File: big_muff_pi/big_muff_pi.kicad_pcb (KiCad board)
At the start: 2 copper layers, 80 x 100 mm, 82 parts, among them J1 Jack_6.35, J2 Jack_6.35, J6 top_panel_connector, J7 Conn_01x01_Socket, J8 Conn_01x01_Socket, J9 Barrel_Jack_Switch, P1 big_muff_pi_front_panel, P2 bottom_panel, Q1 MMBT5551, Q10 AO3401A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

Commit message: small.
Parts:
- P1: value big_muff_pi_front_panel -> front_panel; footprint pedale:big_muff_pi_front_plate -> pedale:front_plate
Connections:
- J1 pad R: 0 -> unconnected-(J1-PadR)
- J2 pad R: 0 -> unconnected-(J2-PadR)
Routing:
- net BAT+: track 15.5 -> 5.66 mm
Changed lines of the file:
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@@
 	(net 48 "REG_IN")
 	(net 49 "Net-(Q12-D)")
+	(net 50 "unconnected-(J1-PadR)")
+	(net 51 "unconnected-(J2-PadR)")
 	(footprint "Resistor_SMD:R_0603_1608Metric_Pad0.98x0.95mm_HandSolder"
 		(layer "F.Cu")
@@
 			(net 43 "unconnected-(J6G-Pin_11-Pad11)")
 			(pinfunction "Pin_11")
-			(pintype "passive")
+			(pintype "passive+no_connect")
 		)
 		(pad "12" thru_hole circle
@@
 			(net 44 "unconnected-(J6G-Pin_13-Pad13)")
 			(pinfunction "Pin_13")
-			(pintype "passive")
+			(pintype "passive+no_connect")
 		)
 		(pad "14" thru_hole circle
@@
 			(net 45 "unconnected-(J6G-Pin_15-Pad15)")
 			(pinfunction "Pin_15")
-			(pintype "passive")
+			(pintype "passive+no_connect")
 		)
 		(pad "16" thru_hole circle
@@
 			(remove_unused_layers no)
 			(roundrect_rratio 0.3)
-			(net 13 "0")
+			(net 51 "unconnected-(J2-PadR)")
 			(pintype "passive")
 			(thermal_bridge_angle 45)
@@
 			(remove_unused_layers no)
 			(roundrect_rratio 0.3)
-			(net 13 "0")
+			(net 50 "unconnected-(J1-PadR)")
 			(pintype "passive")
 			(thermal_bridge_angle 45)
@@
 		(embedded_fonts no)
 	)
-	(footprint "pedale:big_muff_pi_front_plate"
+	(footprint "pedale:front_plate"
 		(layer "F.Cu")
 		(at 50 50)
@@
 			)
 		)
-		(property "Value" "big_muff_pi_front_panel"
+		(property "Value" "front_panel"
 			(at 0 1 0)
 			(unlocked yes)
@@
 	)
 	(segment
-		(start 68.9 89.48185)
-		(end 69.16815 89.75)
-		(width 0.5)
-		(layer "F.Cu")
-		(net 24)
-	)
-	(segment
 		(start -8 107.5)
 		(end -7 108.5)
@@
 	)
 	(segment
-		(start 74.9 89.75)
-		(end 75 89.65)
-		(width 0.5)
-		(layer "F.Cu")
-		(net 24)
-	)
-	(segment
-		(start 68.9 85.9)
-		(end 68.9 89.48185)
-		(width 0.5)
-		(layer "F.Cu")
-		(net 24)
-	)
-	(segment
 		(start -8.65 107.5)
 		(end -8 107.5)
@@
 		(width 0.5)
 		(layer "F.Cu")
-		(net 24)
-	)
-	(segment
-		(start 69.16815 89.75)
-		(end 74.9 89.75)
-		(width 0.5)
-		(layer "F.Cu")

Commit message: I LOVE U
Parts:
- moved C14 74.1 mm to (61.8, 99.5)
- moved C16 74.1 mm to (62.7, 93.6)
- moved C17 74.1 mm to (62.7, 91.9)
- moved C18 74.1 mm to (61.8, 101.0)
- moved C19 74.1 mm to (56.5, 92.5)
- moved C20 74.1 mm to (58.5, 104.6)
- moved Q5 74.1 mm to (60.0, 96.9)
- moved R24 74.1 mm to (56.6, 100.2)
- moved R27 44.6 mm to (62.5, 83.8)
- moved Q6 42.9 mm to (59.5, 76.0), turned to 90 degrees
- moved R23 41.1 mm to (59.5, 79.5), turned to 180 degrees
- moved Q12 39.7 mm to (58.8, 82.8), turned to 90 degrees
- moved R25 27.3 mm to (107.5, 52.0), turned to 180 degrees
- moved R26 20.0 mm to (101.8, 72.2)
- moved C2 2.12 mm to (76.4, 68.1)
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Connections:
- Q6 pad 2: REG_IN -> BAT+
- Q6 pad 3: BAT+ -> REG_IN
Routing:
- net IN_CONNECT: track 0.00 -> 121.5 mm, vias 0 -> 2
- net 9V: track 111.7 -> 214.8 mm, vias 5 -> 6
- net SW_IN: track 22.0 -> 103.7 mm, vias 4 -> 7
- net Net-(SW1B-B): track 0.00 -> 62.0 mm, vias 2 -> 0
- net BAT-: track 0.00 -> 60.1 mm, vias 0 -> 1
- net Net-(J6C-Pin_14): track 20.7 -> 76.6 mm, vias 4 -> 3
- net Net-(J6D-Pin_8): track 0.00 -> 37.1 mm, vias 0 -> 1
- net Net-(J6A-Pin_4): track 5.21 -> 38.8 mm
- net Net-(SW1A-B): track 0.00 -> 28.3 mm
- net BAT+: track 5.66 -> 31.1 mm
- net Net-(J6C-Pin_12): track 2.64 -> 26.4 mm
- net F_OUT: track 0.00 -> 21.8 mm
- net REG_IN: track 26.9 -> 47.2 mm
- net Net-(J6E-Pin_10): track 0.00 -> 17.2 mm
- net FS_OUT: track 0.00 -> 12.7 mm
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
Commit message: small mods.
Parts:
- removed SIM1: Logo_Open_Hardware_Small, Symbol:OSHW-Logo2_7.3x6mm_SilkScreen
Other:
- board text removed: "BMF"
- board text removed: "ostojaatanasijevic"

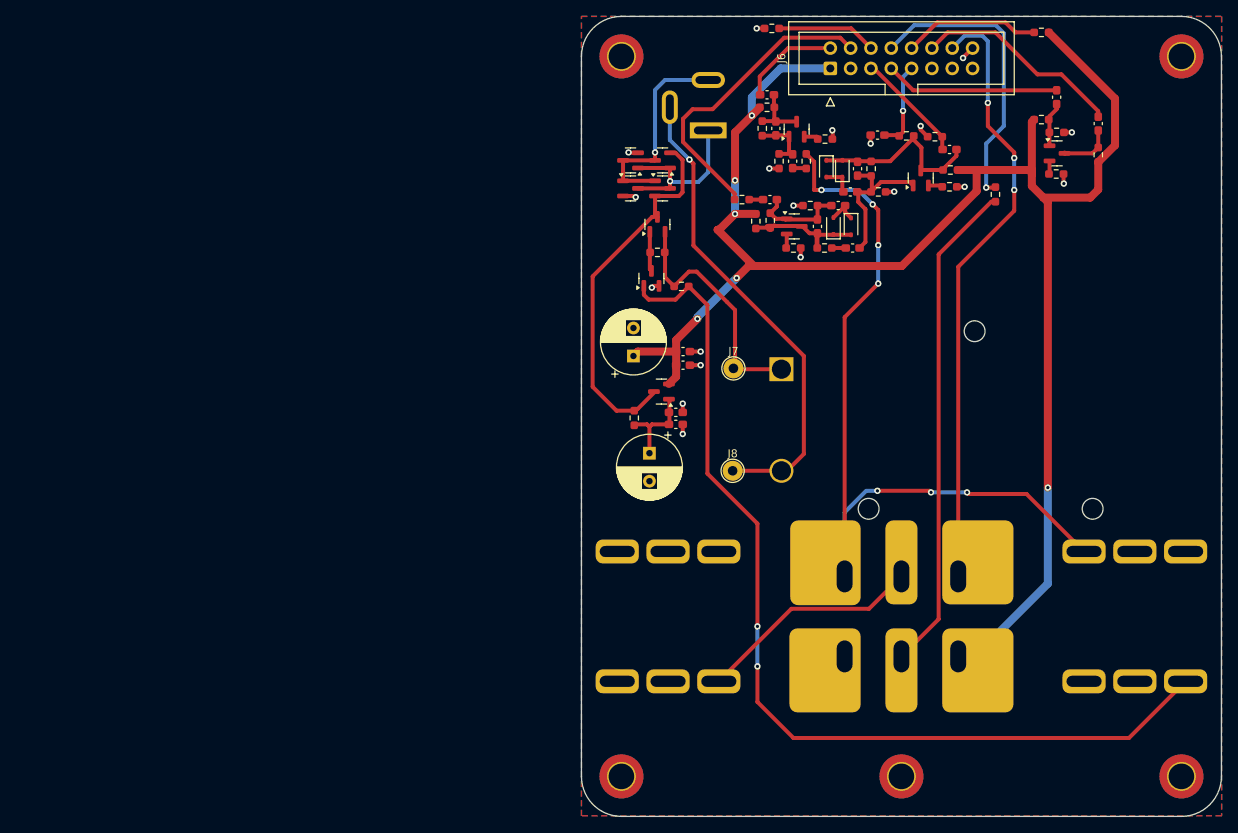
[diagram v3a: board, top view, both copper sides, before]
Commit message: New switch, fixed courtyards.
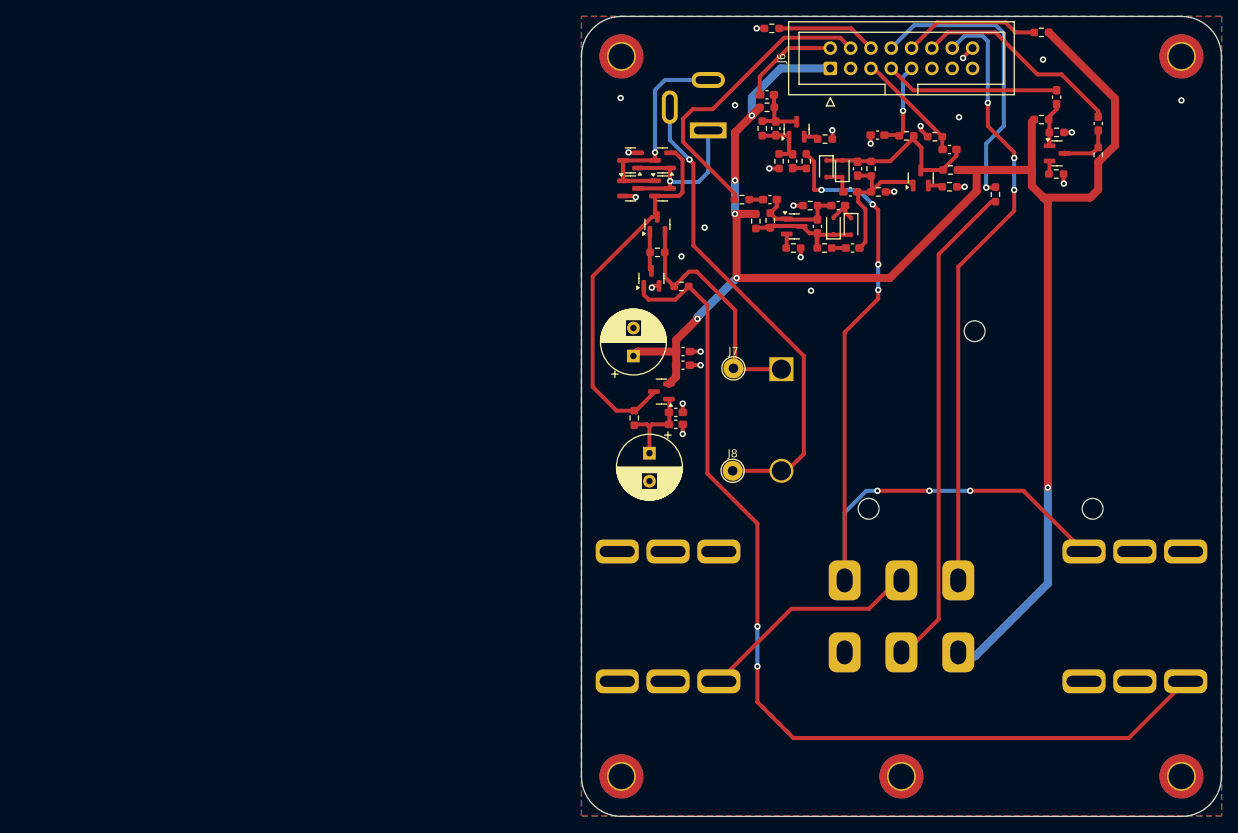
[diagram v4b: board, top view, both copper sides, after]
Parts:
- removed RV4, RV5, RV6: floating_pot, pedale:floating_pot
- SW1: footprint pedale:foot_switch_tht_and_floating -> pedale:foot_switch_tht_no_pad
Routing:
- net 9V: track 214.8 -> 213.5 mm
- net 0: vias 19 -> 27

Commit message: Updated traces.
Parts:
- moved Q10 3.57 mm to (56.7, 68.8)
- moved Q13 3.57 mm to (52.7, 72.3)
- moved Q14 3.57 mm to (52.7, 68.8)
- moved Q8 3.57 mm to (56.7, 72.3)
- moved R27 1.33 mm to (61.4, 84.5), turned to -90 degrees
- moved R23 0.45 mm to (59.7, 79.9)
- moved Q6 0.32 mm to (59.6, 76.3)
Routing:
- net IN_CONNECT: track 121.5 -> 111.1 mm
- net SW_IN: track 103.7 -> 96.8 mm
- net Net-(J6A-Pin_4): track 38.5 -> 31.7 mm
- net CONN-: track 26.5 -> 29.1 mm, vias 1 -> 0
- net BAT+: track 31.1 -> 29.3 mm
- net 9V: track 213.5 -> 212.5 mm
- net BAT-: track 60.1 -> 60.9 mm, vias 1 -> 0
- net CONN+: track 21.1 -> 21.9 mm
- net Net-(SW1A-B): track 28.3 -> 28.8 mm

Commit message: Main board almost ready.
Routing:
- net 0: track 22.2 -> 20.5 mm, vias 27 -> 29
- net Net-(Q2-B): track 19.2 -> 18.6 mm
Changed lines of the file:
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@@
 			(at 1.27 -6.1 90)
 			(layer "F.SilkS")
+			(hide yes)
 			(effects
 				(font
@@
 			(roundrect_rratio 0.3)
 			(net 49 "unconnected-(J2-PadR)")
-			(pintype "passive")
+			(pintype "passive+no_connect")
 			(thermal_bridge_angle 45)
 		)
@@
 			(roundrect_rratio 0.3)
 			(net 28 "unconnected-(J2-PadRN)")
-			(pintype "passive")
+			(pintype "passive+no_connect")
 			(thermal_bridge_angle 45)
 		)
@@
 			(roundrect_rratio 0.3)
 			(net 27 "unconnected-(J2-PadSN)")
-			(pintype "passive")
+			(pintype "passive+no_connect")
 			(thermal_bridge_angle 45)
 		)
@@
 			(roundrect_rratio 0.3)
 			(net 26 "unconnected-(J2-PadTN)")
-			(pintype "passive")
+			(pintype "passive+no_connect")
 			(thermal_bridge_angle 45)
 		)
@@
 			(roundrect_rratio 0.3)
 			(net 48 "unconnected-(J1-PadR)")
-			(pintype "passive")
+			(pintype "passive+no_connect")
 			(thermal_bridge_angle 45)
 		)
@@
 			(roundrect_rratio 0.3)
 			(net 22 "unconnected-(J1-PadRN)")
-			(pintype "passive")
+			(pintype "passive+no_connect")
 			(thermal_bridge_angle 45)
 		)
@@
 			(roundrect_rratio 0.3)
 			(net 23 "unconnected-(J1-PadTN)")
-			(pintype "passive")
+			(pintype "passive+no_connect")
 			(thermal_bridge_angle 45)
 		)
@@
 			(at 0 -2.148 0)
 			(layer "F.SilkS")
+			(hide yes)
 			(effects
 				(font
@@
 			(at 0 -2.148 0)
 			(layer "F.SilkS")
+			(hide yes)
 			(effects
 				(font
@@
 	)
 	(segment
-		(start 97.7 55.1525)
-		(end 98.89 53.9625)
-		(width 0.5)
-		(layer "F.Cu")
-		(net 13)
-	)
-	(segment
 		(start 52.4625 67.85)
 		(end 52.4125 67.8)
@@
 	)
 	(segment
-		(start 97.7 55.2)
-		(end 97.7 55.1525)
-		(width 0.5)
-		(layer "F.Cu")
-		(net 13)
-	)
-	(segment
 		(start 92.4 63.7)
 		(end 92.4 64.1625)
@@
 	)
 	(via
+		(at 89.8 69.3)
+		(size 0.8)
+		(drill 0.4)
+		(layers "F.Cu" "B.Cu")
+		(free yes)
+		(net 13)
+	)
+	(via
 		(at 89.1 71.9)
 		(size 0.8)
@@
 	)
 	(via
-		(at 97.7 55.2)
+		(at 106.7 60.7)
+		(size 0.8)
+		(drill 0.4)
+		(layers "F.Cu" "B.Cu")
+		(free yes)
+		(net 13)
+	)
+	(via
+		(at 105.6 57.8)
 		(size 0.8)
 		(drill 0.4)
@@
 	)
 	(segment
-		(start 61.8375 91.897349)
-		(end 61.8375 90.4625)
-		(width 1)
-		(layer "F.Cu")
-		(net 14)
-	)
-	(segment
 		(start 106.3 63.1875)
 		(end 106.3 69.8)
@@
 	)
 	(segment
-		(start 61.8375 90.4625)
-		(end 64.5 87.8)
-		(width 1)
-		(layer "F.Cu")
-		(net 14)
-	)
-	(segment
-		(start 71.4 80.8)
-		(end 69.4 78.8)
+		(start 64.2 87.9)
+		(end 61.8375 90.2625)
 		(width 1)
 		(layer "F.Cu")
@@
 	)
 	(segment
-		(start 69.4 78.8)
-		(end 69.4 74.8875)
+		(start 71.4 80.8)
+		(end 69.2 78.6)
+		(width 1)
+		(layer "F.Cu")
+		(net 14)
+	)
+	(segment
+		(start 69.2 78.6)
+		(end 69.2 74.6875)
 		(width 1)
 		(layer "F.Cu")
@@
 	)
 	(segment
+		(start 61.8375 90.2625)
+		(end 61.8375 91.897349)
+		(width 1)
+		(layer "F.Cu")
+		(net 14)
+	)
+	(segment
 		(start 107.75 72.65)
 		(end 113.6 72.65)
@@
 		(net 14)
 	)
-	(segment
-		(start 69.4 74.8875)
-		(end 69.2 74.6875)
-		(width 1)
-		(layer "F.Cu")
-		(net 14)
-	)
 	(via
 		(at 71.4 80.8)
@@
 	)
 	(via
-		(at 64.5 87.8)
+		(at 64.2 87.9)
 		(size 0.8)
 		(drill 0.4)
@@
 	(segment
 		(start 71.3 80.8)
-		(end 64.5 87.6)
+		(end 71.4 80.8)
 		(width 1)
 		(layer "B.Cu")
@@
 	)
 	(segment
-		(start 64.5 87.6)
-		(end 64.5 87.8)
+		(start 64.2 87.9)
+		(end 71.3 80.8)
 		(width 1)
 		(layer "B.Cu")
@@
 	)
 	(segment
-		(start 71.4 80.8)
-		(end 71.3 80.8)
-		(width 1)
-		(layer "B.Cu")
-		(net 14)
-	)
-	(segment
 		(start 71.33 71.06)
 		(end 69.2 73.19)
@@
 	)
 	(segment
-		(start 85.5 78.2125)
-		(end 84.7625 78.95)
+		(start 86 72)
+		(end 84.4 72)
 		(width 0.5)
 		(layer "F.Cu")
@@
 	)
 	(segment
-		(start 86.3 70.1)
-		(end 86.3 71.7)
+		(start 84.8 78.9125)
+		(end 84.7625 78.95)
 		(width 0.5)
 		(layer "F.Cu")
@@
 	)
 	(segment
-		(start 86 72)
-		(end 84.4 72)
+		(start 86.3 71.7)
+		(end 86 72)
 		(width 0.5)
 		(layer "F.Cu")
@@
 	)
 	(segment
-		(start 86.1 69.9)
-		(end 86.3 70.1)
+		(start 84.5125 69.9)
+		(end 86.1 69.9)
 		(width 0.5)
 		(layer "F.Cu")
@@
 	)
 	(segment
-		(start 84.4 72)
-		(end 84.4 73.6)
+		(start 84.8 74)
+		(end 84.8 78.9125)
 		(width 0.5)
 		(layer "F.Cu")
@@
 	)
 	(segment
-		(start 84.5125 69.9)
-		(end 86.1 69.9)
+		(start 84.4 73.6)
+		(end 84.8 74)
 		(width 0.5)
 		(layer "F.Cu")
@@
 	)
 	(segment
-		(start 86.3 71.7)
-		(end 86 72)
+		(start 86.3 70.1)
+		(end 86.3 71.7)
 		(width 0.5)
 		(layer "F.Cu")
@@
 	)
 	(segment
-		(start 85.5 74.7)
-		(end 85.5 78.2125)
+		(start 86.1 69.9)
+		(end 86.3 70.1)
 		(width 0.5)
 		(layer "F.Cu")
@@
 	)
 	(segment
-		(start 84.4 73.6)
-		(end 85.5 74.7)
+		(start 84.4 72)
+		(end 84.4 73.6)
 		(width 0.5)
 		(layer "F.Cu")
@@
 	)
 	(segment
-		(start 63.32 75.960306)
-		(end 78.8 91.440306)
+		(start 63.32 76.62)
+		(end 78.8 92.1)
 		(width 1)
 		(layer "F.Cu")
@@
 	)
 	(segment
-		(start 78.8 91.440306)
-		(end 78.8 103.7)
+		(start 61.05 61.35)
+		(end 61.05 68.3)
 		(width 1)
 		(layer "F.Cu")
@@
 	)
 	(segment
-		(start 63.32 70.57)
-		(end 63.32 75.960306)
+		(start 68.9 106.8)
+		(end 75 106.8)
 		(width 1)
 		(layer "F.Cu")
@@
 	)
 	(segment
-		(start 68.9 106.8)
-		(end 75 106.8)
+		(start 78.8 103.7)
+		(end 75.7 106.8)
 		(width 1)
 		(layer "F.Cu")
@@
 	)
 	(segment
-		(start 78.8 103.7)
-		(end 75.7 106.8)
+		(start 78.8 92.1)
+		(end 78.8 103.7)
 		(width 1)
 		(layer "F.Cu")
@@
 	)
 	(segment
-		(start 75.7 106.8)
-		(end 75 106.8)
+		(start 61.05 68.3)
+		(end 63.32 70.57)
 		(width 1)
 		(layer "F.Cu")
@@
 	)
 	(segment
-		(start 61.05 61.35)
-		(end 61.05 68.3)
+		(start 63.32 70.57)
+		(end 63.32 76.62)
 		(width 1)
 		(layer "F.Cu")
@@
 	)
 	(segment
-		(start 61.05 68.3)
-		(end 63.32 70.57)
+		(start 75.7 106.8)
+		(end 75 106.8)
 		(width 1)
 		(layer "F.Cu")

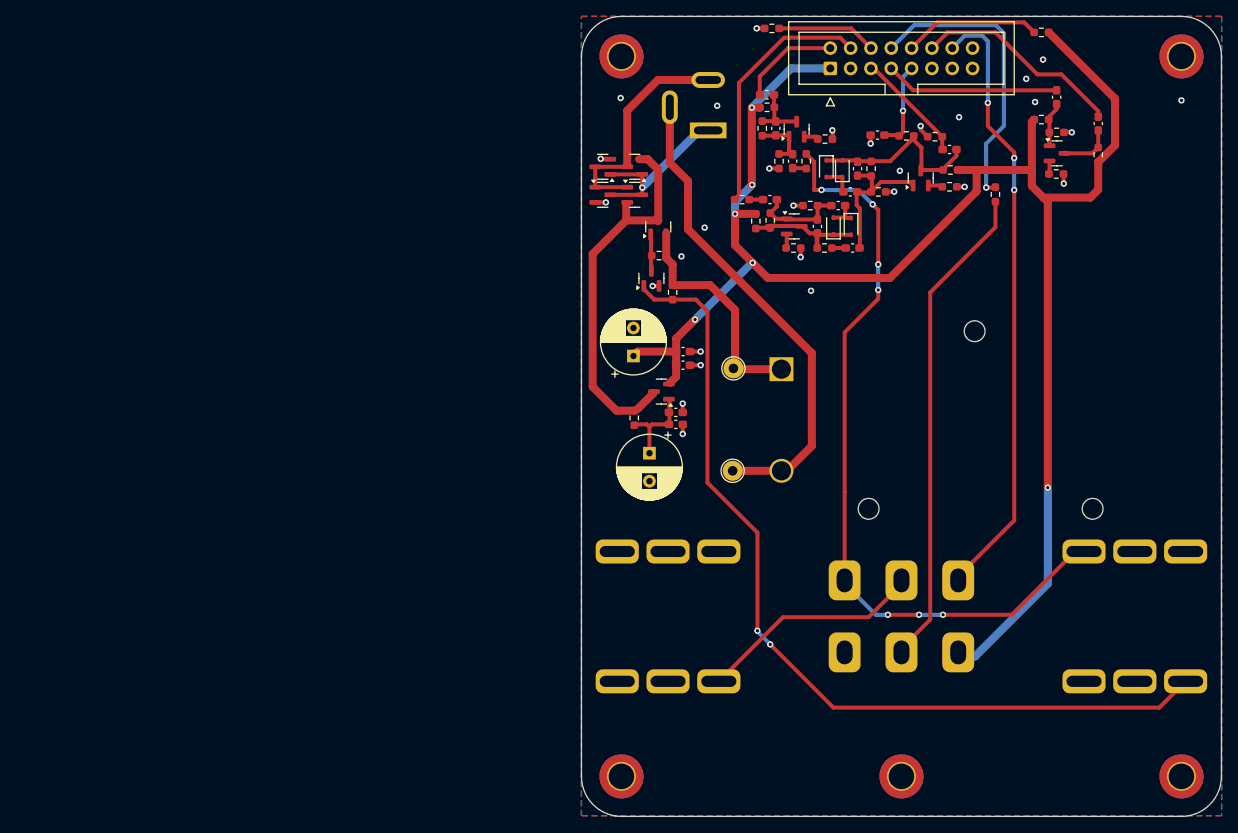
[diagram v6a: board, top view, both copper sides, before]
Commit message: Rounded traces.
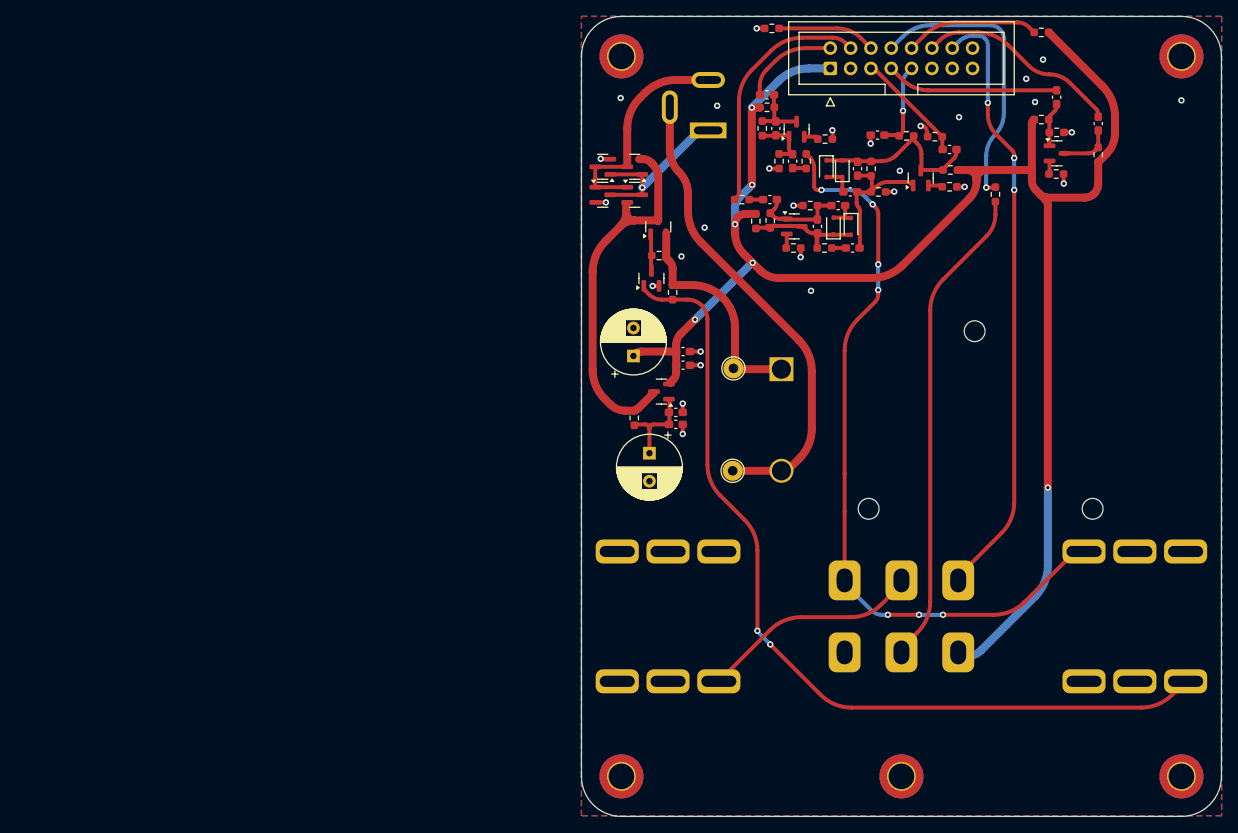
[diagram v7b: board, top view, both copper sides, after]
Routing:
- net IN_CONNECT: track 111.1 -> 109.6 mm
- net REG_IN: track 47.4 -> 48.9 mm
- net SW_IN: track 96.8 -> 95.5 mm
- net BAT-: track 60.9 -> 59.7 mm
- net Net-(J6C-Pin_12): track 26.4 -> 25.6 mm
- net Net-(SW1B-B): track 61.7 -> 60.9 mm
- net Net-(J6D-Pin_8): track 37.1 -> 36.3 mm
- net Net-(J6C-Pin_14): track 76.6 -> 75.8 mm
- net Net-(J6A-Pin_4): track 31.7 -> 31.0 mm
- net BAT+: track 29.3 -> 28.7 mm
- net Net-(SW1A-B): track 28.8 -> 28.3 mm
- net 9V: track 212.5 -> 213.1 mm
- net CONN-: track 29.1 -> 28.6 mm

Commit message: 2.2k LED.
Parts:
- R25, R26: value 1k -> 2.2k
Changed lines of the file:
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@@
 			)
 		)
-		(property "Value" "1k"
+		(property "Value" "2.2k"
 			(at 0 1.43 90)
 			(layer "F.Fab")
@@
 			)
 		)
-		(property "LCSC" "C21190"
+		(property "LCSC" "C4190"
 			(at 0 0 270)
 			(unlocked yes)
@@
 			)
 		)
-		(property "Value" "1k"
+		(property "Value" "2.2k"
 			(at 0 1.43 0)
 			(layer "F.Fab")
@@
 			)
 		)
-		(property "LCSC" "C21190"
+		(property "LCSC" "C4190"
 			(at 0 0 180)
 			(unlocked yes)
